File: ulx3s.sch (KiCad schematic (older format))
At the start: 10 parts, among them U1 LFE5U-25F-6BG381C, U2 ESP-12E

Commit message: Power sheet added OLED header added Moving components and adjusting
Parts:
- removed unit 9 of U1
- AUDIO1: footprint (none) -> Pin_Headers:Pin_Header_Angled_2x03
- OLED1: footprint (none) -> Socket_Strips:Socket_Strip_Straight_1x07
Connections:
- net labels added: SD_CD, SD_WP, WIFI_RXD, WIFI_TXD
- wire segments 193 -> 61
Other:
- moved on the sheet: AUDIO1, D3, D4, GPDI1, U1J, U2, US1, US2

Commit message: add DC-DC converter to power sheet
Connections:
- net labels added: +3V3
- net labels removed: GPDI_5V, VCC
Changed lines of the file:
@@
 LIBS:lfe5bg381
 LIBS:micro-hdmi-d
+LIBS:ap3429a
 LIBS:ulx3s-cache
 EELAYER 25 0
@@
 	0    -1   -1   0
 $EndComp
-$Comp
-L VCC #PWR07
-U 1 1 58D522D3
-P 8200 3750
-F 0 "#PWR07" H 8200 3600 50  0001 C CNN
-F 1 "VCC" H 8200 3900 50  0000 C CNN
-F 2 "" H 8200 3750 50  0000 C CNN
-F 3 "" H 8200 3750 50  0000 C CNN
-	1    8200 3750
-	0    1    1    0
-$EndComp
 Wire Wire Line
 	5400 3650 6100 3650
@@
 Text Label 5450 5250 0    60   ~ 0
 GPDI_SCL
-Text Label 5450 5450 0    60   ~ 0
-GPDI_5V
-Wire Wire Line
-	5400 5450 6100 5450
+Wire Wire Line
+	5400 5450 6300 5450
 Wire Wire Line
 	5400 5350 6100 5350
@@
 	5400 5550 6100 5550
 $Comp
-L GND #PWR08
+L GND #PWR07
 U 1 1 58D544FB
 P 6100 5550
-F 0 "#PWR08" H 6100 5300 50  0001 C CNN
+F 0 "#PWR07" H 6100 5300 50  0001 C CNN
 F 1 "GND" H 6100 5400 50  0000 C CNN
 F 2 "" H 6100 5550 60  0000 C CNN
@@
 $EndComp
 $Comp
-L GND #PWR09
+L GND #PWR08
 U 1 1 58D5464C
 P 6100 5150
-F 0 "#PWR09" H 6100 4900 50  0001 C CNN
+F 0 "#PWR08" H 6100 4900 50  0001 C CNN
 F 1 "GND" H 6100 5000 50  0000 C CNN
 F 2 "" H 6100 5150 60  0000 C CNN
@@
 $EndComp
 $Comp
-L GND #PWR010
+L GND #PWR09
 U 1 1 58D54683
 P 6100 4850
-F 0 "#PWR010" H 6100 4600 50  0001 C CNN
+F 0 "#PWR09" H 6100 4600 50  0001 C CNN
 F 1 "GND" H 6100 4700 50  0000 C CNN
 F 2 "" H 6100 4850 60  0000 C CNN
@@
 $EndComp
 $Comp
-L GND #PWR011
+L GND #PWR010
 U 1 1 58D54712
 P 6100 4550
-F 0 "#PWR011" H 6100 4300 50  0001 C CNN
+F 0 "#PWR010" H 6100 4300 50  0001 C CNN
 F 1 "GND" H 6100 4400 50  0000 C CNN
 F 2 "" H 6100 4550 60  0000 C CNN
@@
 $EndComp
 $Comp
-L GND #PWR012
+L GND #PWR011
 U 1 1 58D54749
 P 6100 4250
-F 0 "#PWR012" H 6100 4000 50  0001 C CNN
+F 0 "#PWR011" H 6100 4000 50  0001 C CNN
 F 1 "GND" H 6100 4100 50  0000 C CNN
 F 2 "" H 6100 4250 60  0000 C CNN
@@
 $EndComp
 $Comp
-L GND #PWR013
+L GND #PWR012
 U 1 1 58D547C2
 P 6100 3950
-F 0 "#PWR013" H 6100 3700 50  0001 C CNN
+F 0 "#PWR012" H 6100 3700 50  0001 C CNN
 F 1 "GND" H 6100 3800 50  0000 C CNN
 F 2 "" H 6100 3950 60  0000 C CNN
@@
 F1 "power.sch" 60
 $EndSheet
-$Comp
-L VCC #PWR014
-U 1 1 58D57623
-P 2250 4950
-F 0 "#PWR014" H 2250 4800 50  0001 C CNN
-F 1 "VCC" H 2250 5100 50  0000 C CNN
-F 2 "" H 2250 4950 50  0000 C CNN
-F 3 "" H 2250 4950 50  0000 C CNN
-	1    2250 4950
-	0    -1   -1   0
-$EndComp
 Wire Wire Line
 	2250 4950 2300 4950
@@
 	1050 6800 1400 6800
 $Comp
-L VCC #PWR015
-U 1 1 58D58165
-P 900 6600
-F 0 "#PWR015" H 900 6450 50  0001 C CNN
-F 1 "VCC" H 900 6750 50  0000 C CNN
-F 2 "" H 900 6600 50  0000 C CNN
-F 3 "" H 900 6600 50  0000 C CNN
-	1    900  6600
-	0    -1   -1   0
-$EndComp
-$Comp
-L GND #PWR016
+L GND #PWR013
 U 1 1 58D58197
 P 1050 6500
-F 0 "#PWR016" H 1050 6250 50  0001 C CNN
+F 0 "#PWR013" H 1050 6250 50  0001 C CNN
 F 1 "GND" H 1050 6350 50  0000 C CNN
 F 2 "" H 1050 6500 50  0000 C CNN
@@
 $EndComp
 $Comp
-L GND #PWR017
+L GND #PWR014
 U 1 1 58D581BF
 P 1050 6800
-F 0 "#PWR017" H 1050 6550 50  0001 C CNN
+F 0 "#PWR014" H 1050 6550 50  0001 C CNN
 F 1 "GND" H 1050 6650 50  0000 C CNN
 F 2 "" H 1050 6800 50  0000 C CNN
@@
 SD_WP
 $Comp
-L GND #PWR018
+L GND #PWR015
 U 1 1 58D58733
 P 3300 6900
-F 0 "#PWR018" H 3300 6650 50  0001 C CNN
+F 0 "#PWR015" H 3300 6650 50  0001 C CNN
 F 1 "GND" H 3300 6750 50  0000 C CNN
 F 2 "" H 3300 6900 50  0000 C CNN
@@
 	3200 6800 3300 6800
 Connection ~ 3300 6800
+$Comp
+L +3V3 #PWR016
+U 1 1 58D5F08C
+P 2250 4950
+F 0 "#PWR016" H 2250 4800 50  0001 C CNN
+F 1 "+3V3" H 2250 5090 50  0000 C CNN
+F 2 "" H 2250 4950 50  0000 C CNN
+F 3 "" H 2250 4950 50  0000 C CNN
+	1    2250 4950
+	0    -1   -1   0
+$EndComp
+$Comp
+L +3V3 #PWR017
+U 1 1 58D5F123
+P 900 6600
+F 0 "#PWR017" H 900 6450 50  0001 C CNN
+F 1 "+3V3" H 900 6740 50  0000 C CNN
+F 2 "" H 900 6600 50  0000 C CNN
+F 3 "" H 900 6600 50  0000 C CNN
+	1    900  6600
+	0    -1   -1   0
+$EndComp
+$Comp
+L +5V #PWR018
+U 1 1 58D5F259
+P 6300 5450
+F 0 "#PWR018" H 6300 5300 50  0001 C CNN
+F 1 "+5V" H 6300 5590 50  0000 C CNN
+F 2 "" H 6300 5450 50  0000 C CNN
+F 3 "" H 6300 5450 50  0000 C CNN
+	1    6300 5450
+	0    1    1    0
+$EndComp
+$Comp
+L +3V3 #PWR019
+U 1 1 58D5F30F
+P 8200 3750
+F 0 "#PWR019" H 8200 3600 50  0001 C CNN
+F 1 "+3V3" H 8200 3890 50  0000 C CNN
+F 2 "" H 8200 3750 50  0000 C CNN
+F 3 "" H 8200 3750 50  0000 C CNN
+	1    8200 3750
+	0    1    1    0
+$EndComp
 $EndSCHEMATC

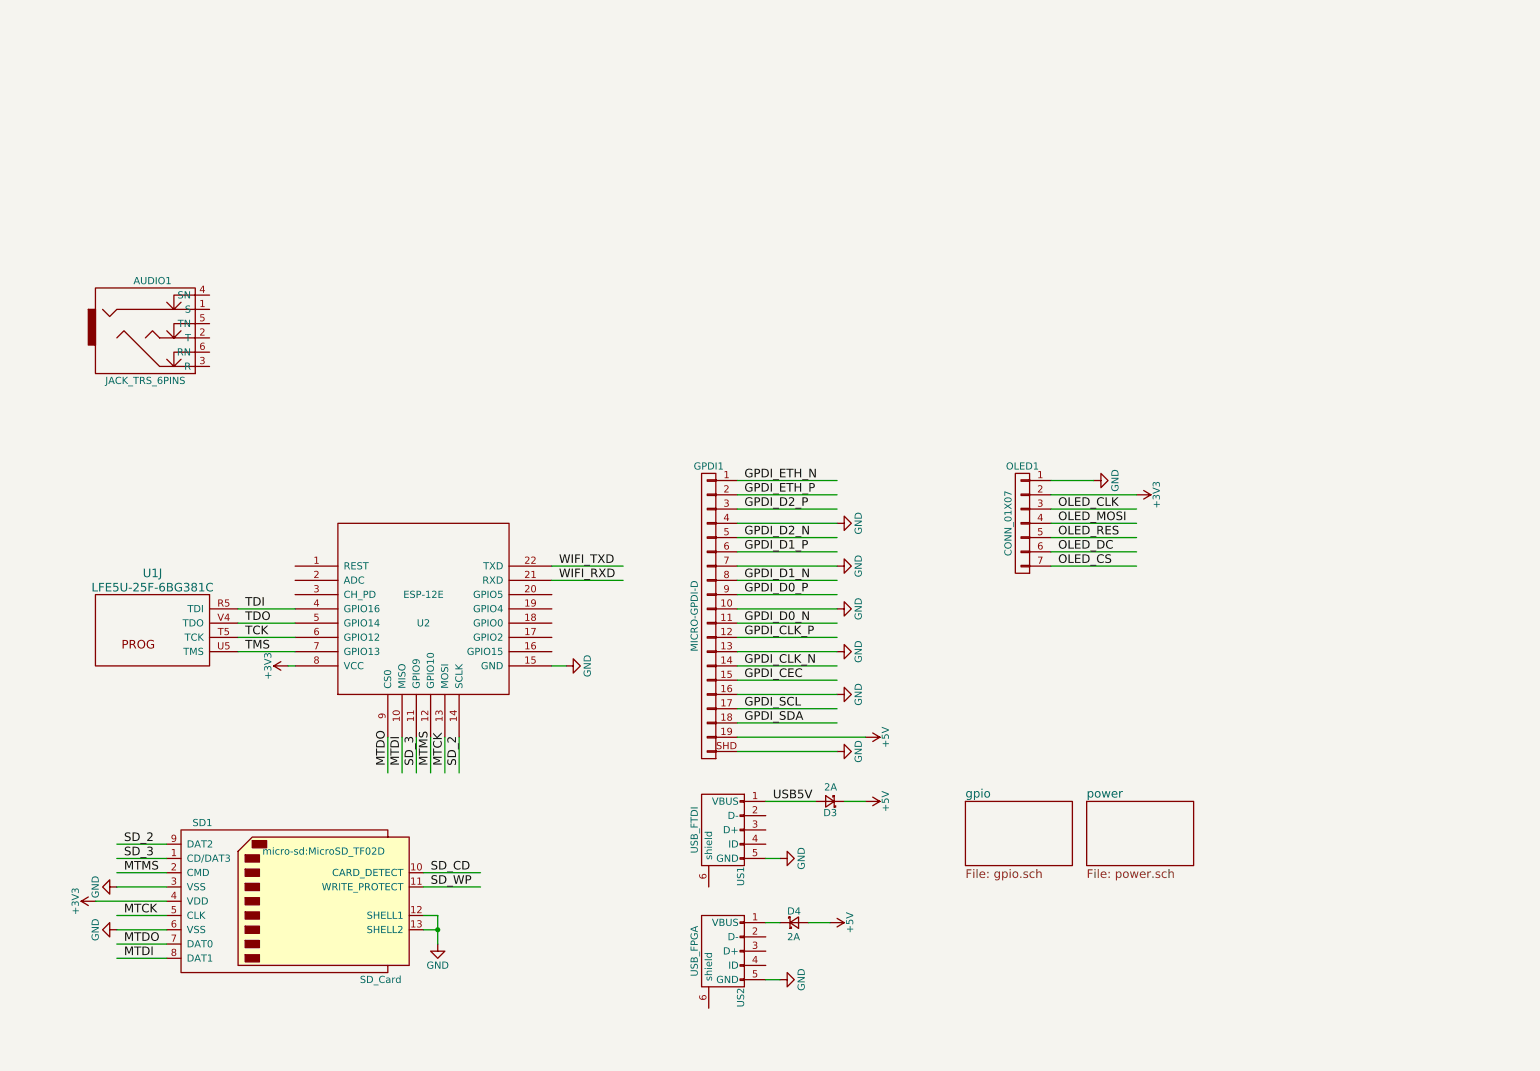
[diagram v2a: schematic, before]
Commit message: add push buttons
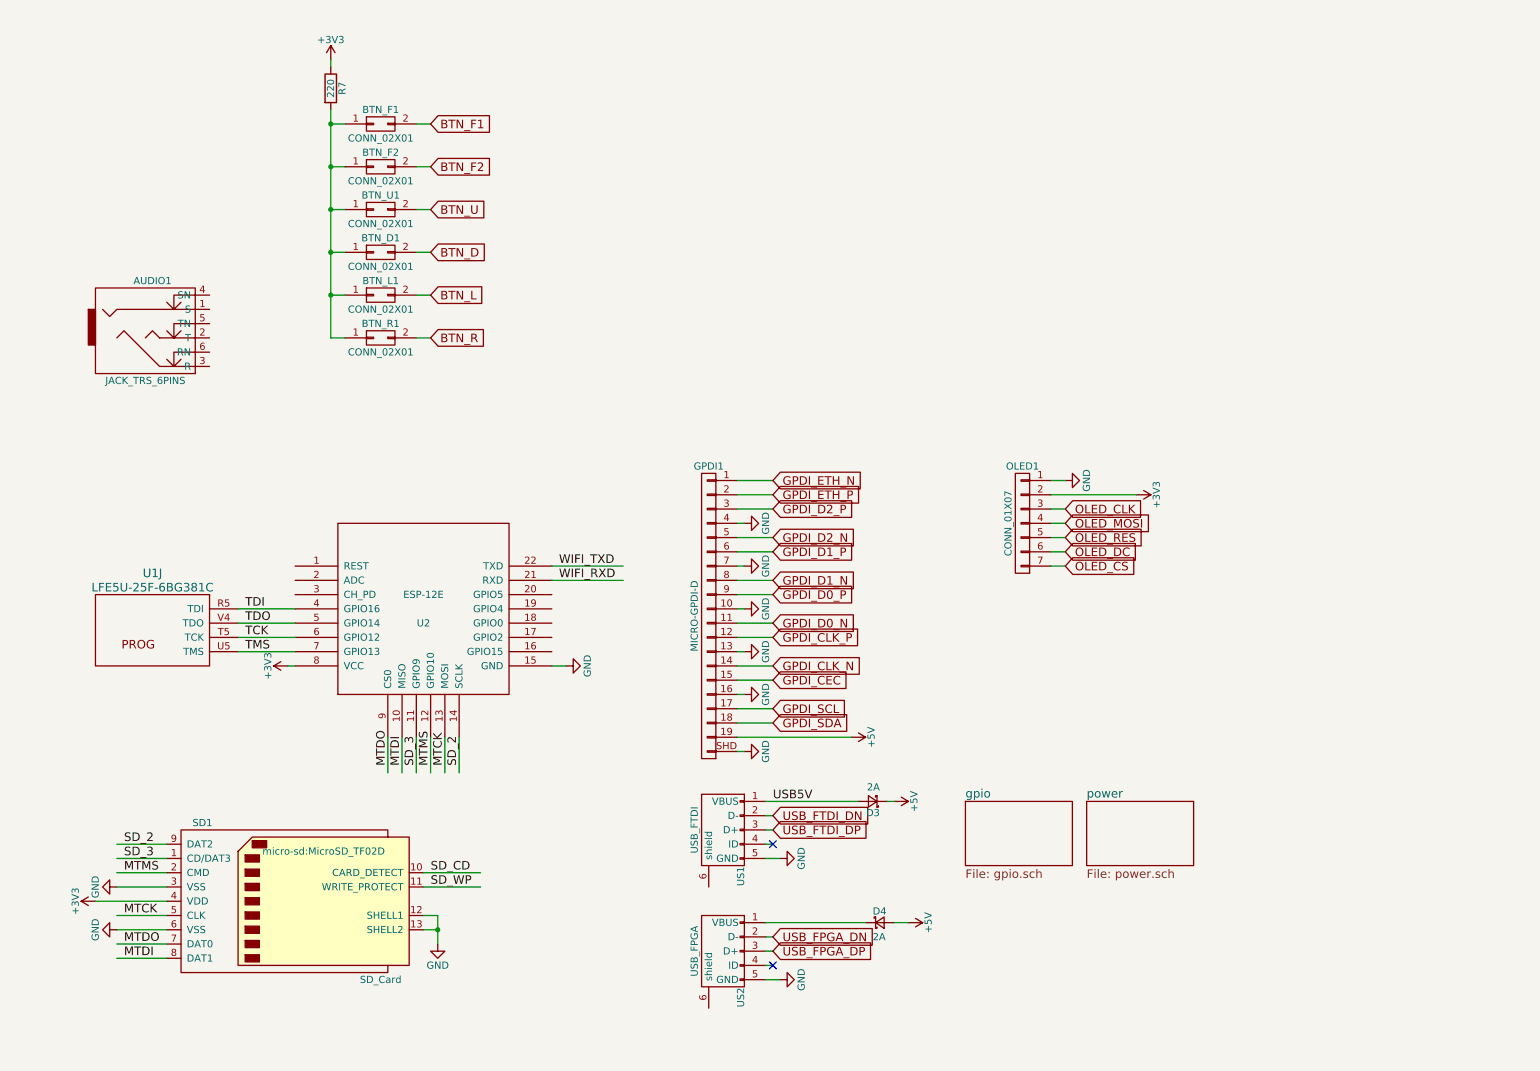
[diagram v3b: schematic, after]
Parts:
- added BTN_D1, BTN_F1, BTN_F2, BTN_L1, BTN_R1, BTN_U1: CONN_02X01, Buttons_Switches_SMD:SW_SPST_SKQG, symbol CONN_02X01
- added R7: 220, Resistors_SMD:R_0805_HandSoldering, symbol R
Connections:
- net labels added: BTN_D, BTN_F1, BTN_F2, BTN_L, BTN_R, BTN_U, USB_FPGA_DN, USB_FPGA_DP, USB_FTDI_DN, USB_FTDI_DP
- wire segments 61 -> 81
- no-connect marks 0 -> 2
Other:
- moved on the sheet: D3, D4

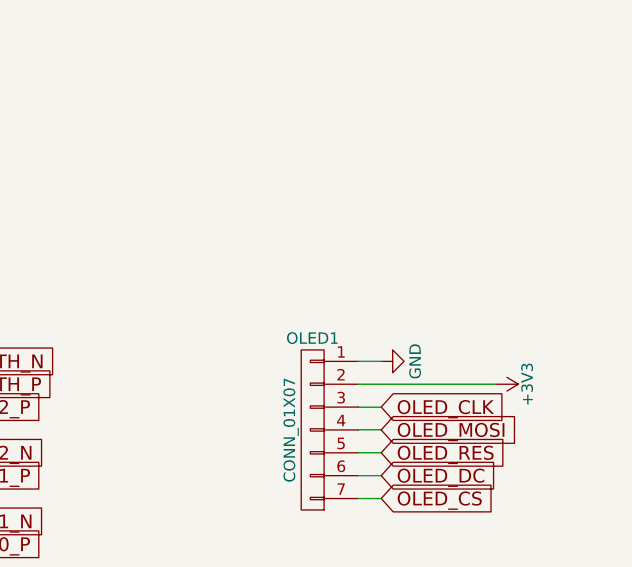
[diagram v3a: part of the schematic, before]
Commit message: rearrange OLED and buttons
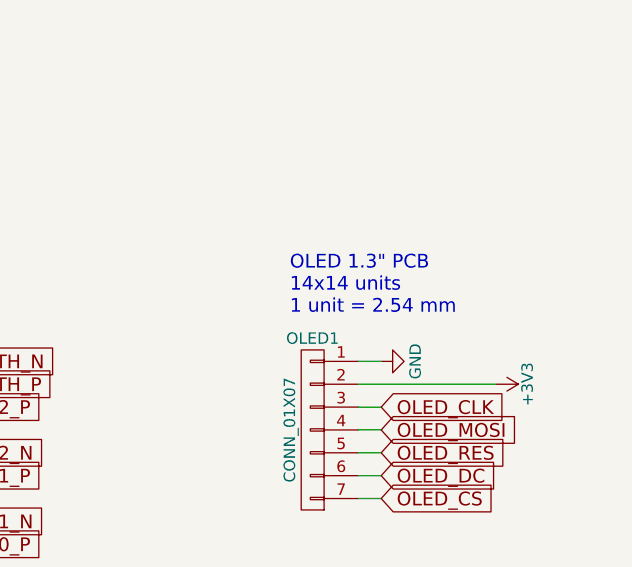
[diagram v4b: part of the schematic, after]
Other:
- note added: "OLED 1.3" PCB \n14x14 units\n1 unit = 2.54 mm"
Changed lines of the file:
@@
 Wire Wire Line
 	2550 700  2550 750
+Text Notes 7300 3450 0    60   ~ 0
+OLED 1.3" PCB \n14x14 units\n1 unit = 2.54 mm
 $EndSCHEMATC

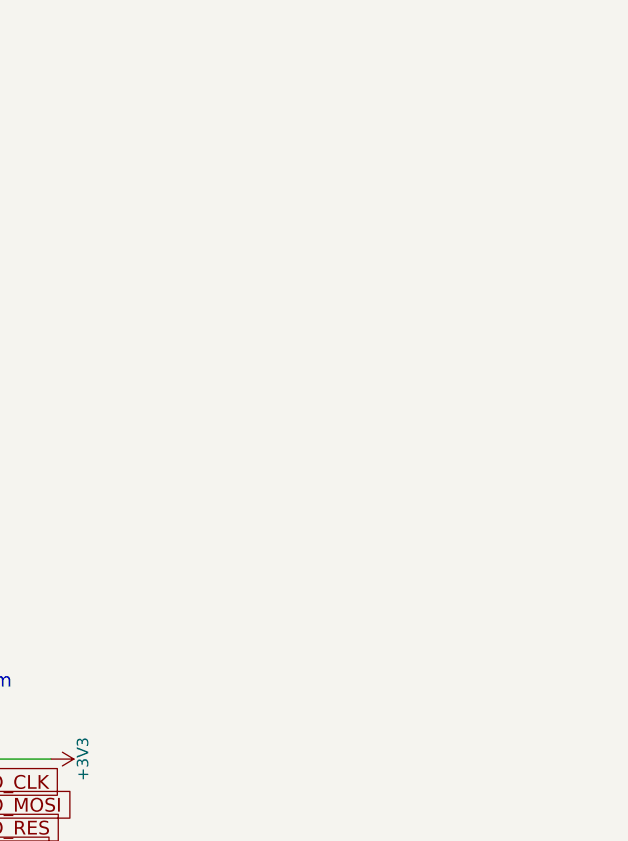
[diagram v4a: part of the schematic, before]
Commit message: add SDRAM chip (probably wrong footprint)
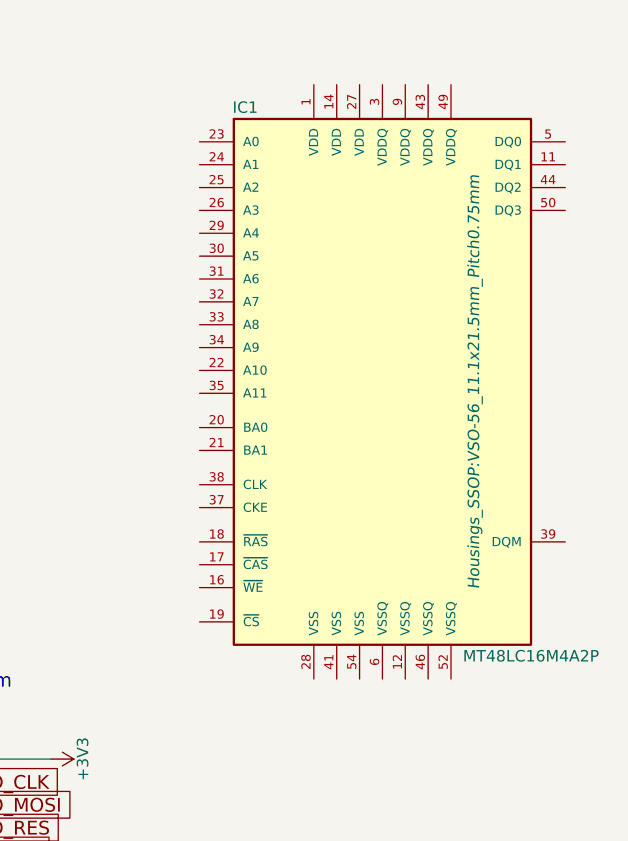
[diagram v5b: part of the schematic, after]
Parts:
- added IC1: MT48LC16M4A2P, Housings_SSOP:VSO-56_11.1x21.5mm_Pitch0.75mm, symbol MT48LC16M4A2P
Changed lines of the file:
@@
 Text Notes 7300 3450 0    60   ~ 0
 OLED 1.3" PCB \n14x14 units\n1 unit = 2.54 mm
+$Comp
+L MT48LC16M4A2P IC1
+U 1 1 58D5C787
+P 9650 2100
+F 0 "IC1" H 9050 3300 50  0000 C CNN
+F 1 "MT48LC16M4A2P" H 10300 900 50  0000 C CNN
+F 2 "Housings_SSOP:VSO-56_11.1x21.5mm_Pitch0.75mm" V 10050 2100 50  0000 C CIN
+F 3 "" H 9650 1850 50  0000 C CNN
+	1    9650 2100
+	1    0    0    -1
+$EndComp
 $EndSCHEMATC

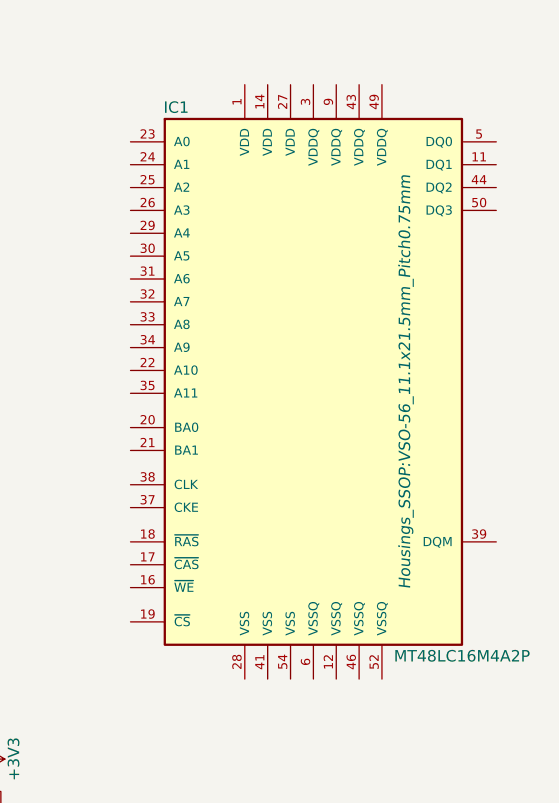
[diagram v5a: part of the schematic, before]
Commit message: added SDRAM TSOP-54 package
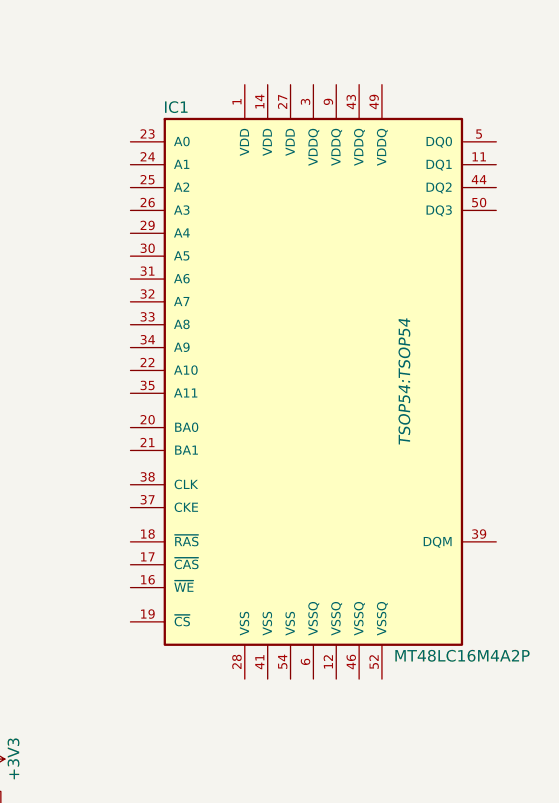
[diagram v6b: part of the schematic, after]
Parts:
- IC1: footprint Housings_SSOP:VSO-56_11.1x21.5mm_Pitch0.75mm -> TSOP54:TSOP54
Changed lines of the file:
@@
 F 0 "IC1" H 9050 3300 50  0000 C CNN
 F 1 "MT48LC16M4A2P" H 10300 900 50  0000 C CNN
-F 2 "Housings_SSOP:VSO-56_11.1x21.5mm_Pitch0.75mm" V 10050 2100 50  0000 C CIN
+F 2 "TSOP54:TSOP54" V 10050 2100 50  0000 C CIN
 F 3 "" H 9650 1850 50  0000 C CNN
 	1    9650 2100
